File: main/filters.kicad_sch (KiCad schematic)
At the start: 104 parts, among them U36 TL071, U37 LM13700, U38 TL071, U39 TL071, U40 TL071, U41 LM13700, U42 LM13700, U43 LM13700

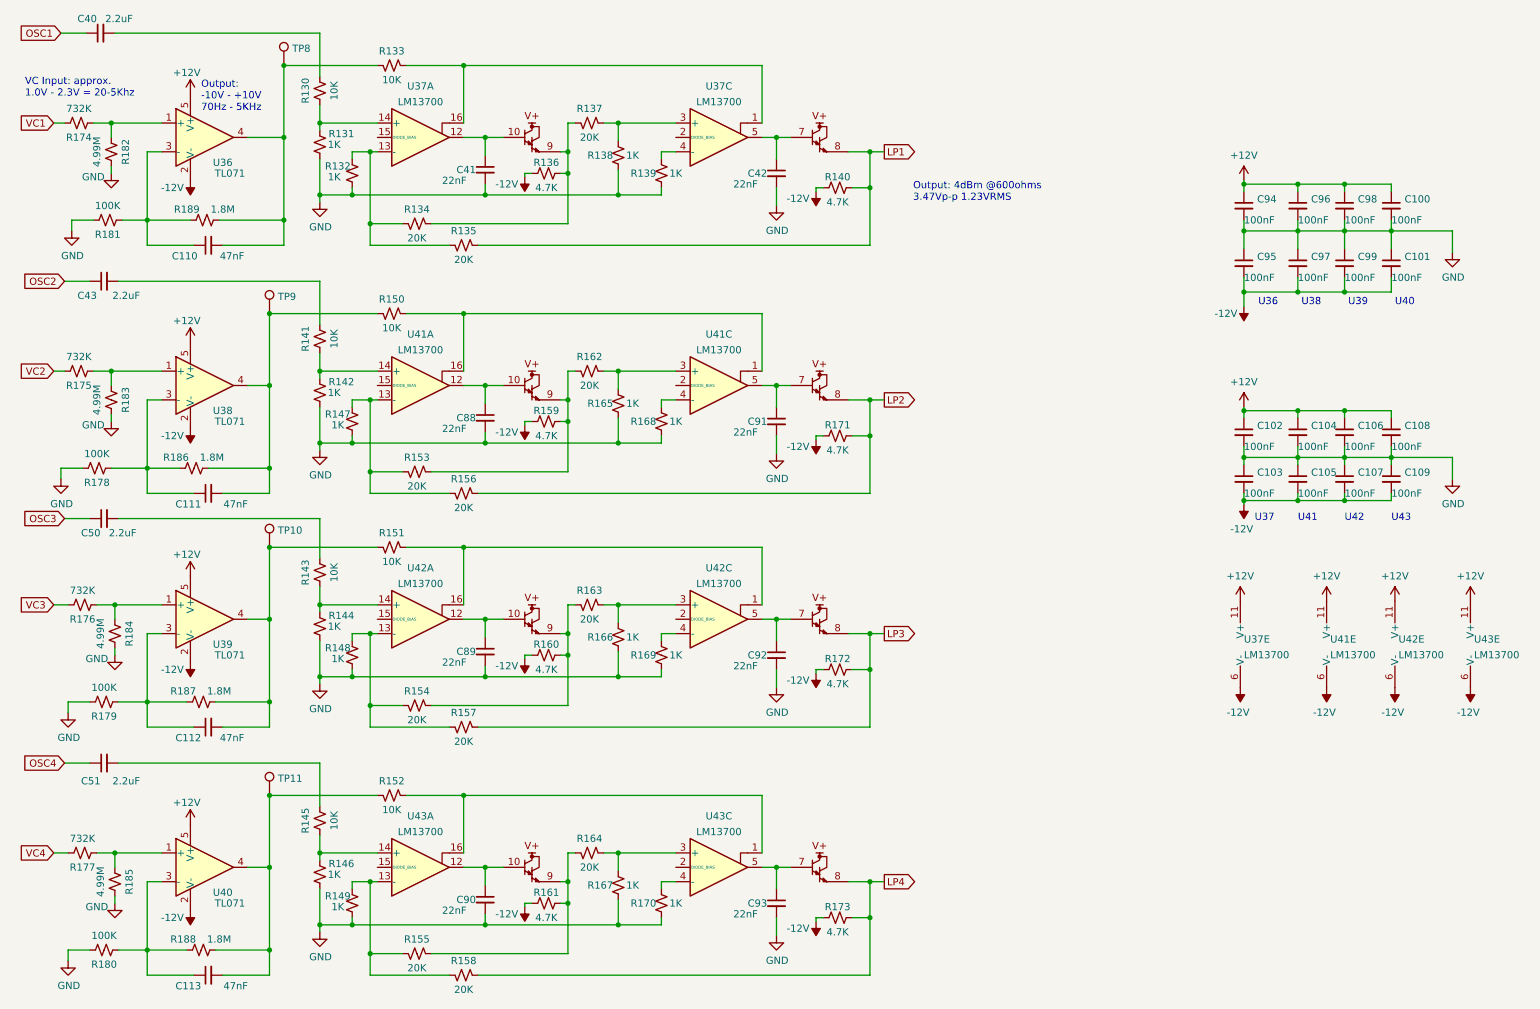
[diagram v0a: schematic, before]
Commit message: v1.0
Docs still need work.
Oscillators.sch not used. Saved just in case.
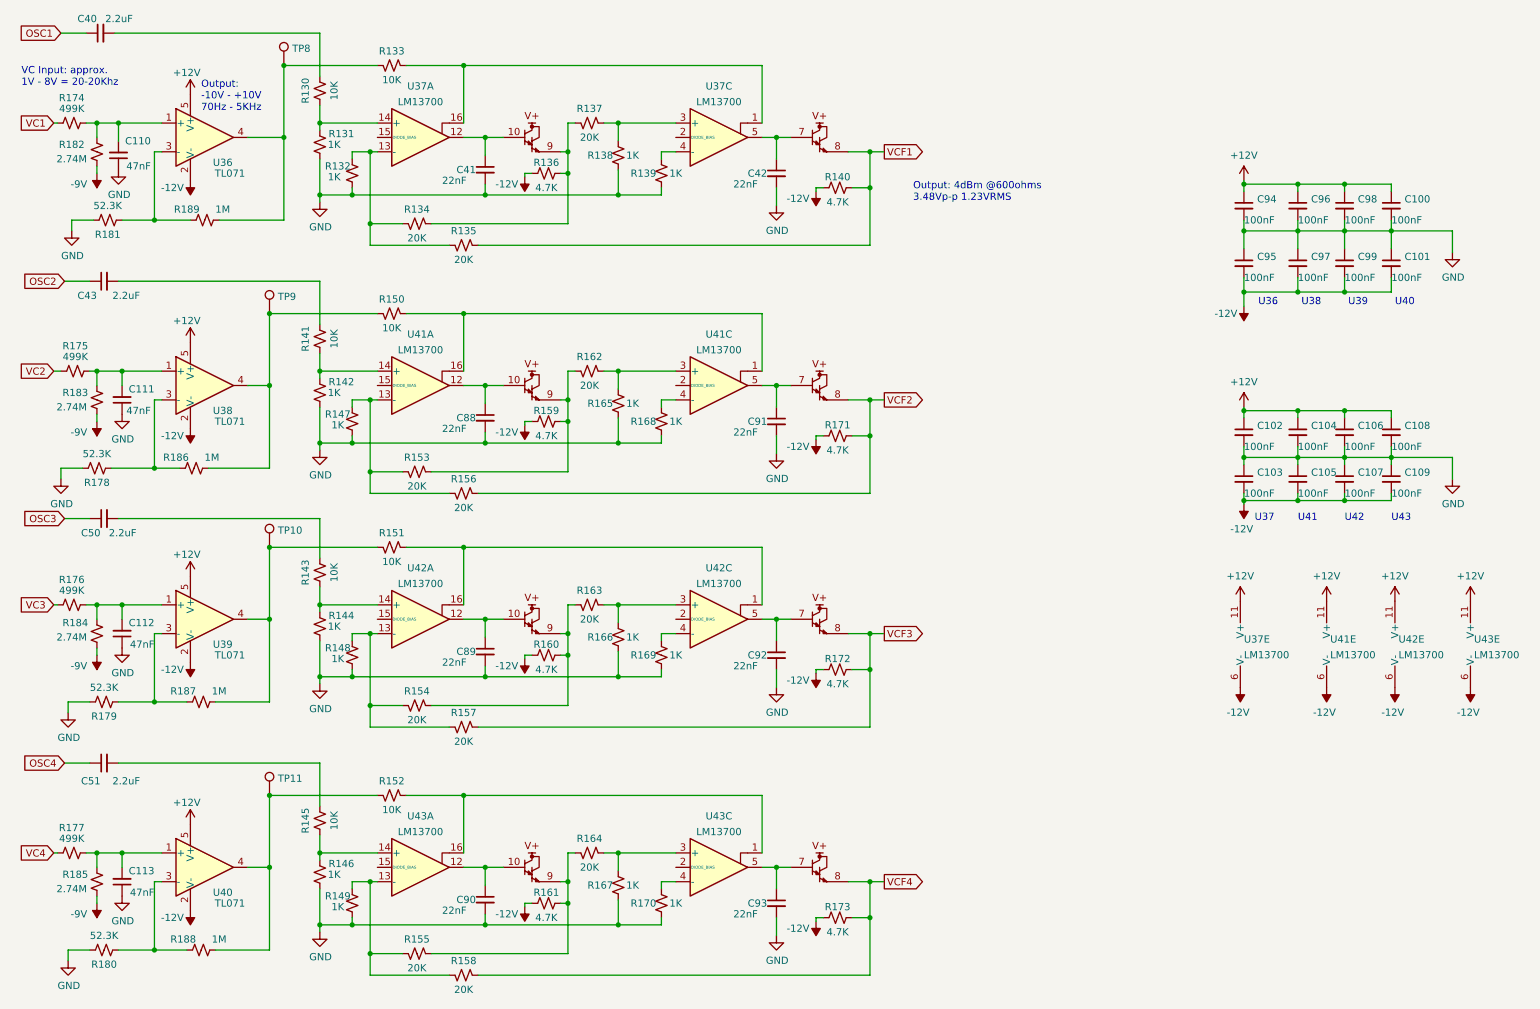
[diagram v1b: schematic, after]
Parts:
- C110, C111, C112, C113: footprint Capacitor_SMD:C_0805_2012Metric_Pad1.18x1.45mm_HandSolder -> Capacitor_SMD:C_0603_1608Metric_Pad1.08x0.95mm_HandSolder; LCSC Part # C53134 -> C1622
- R174, R175, R176, R177: value 732K -> 499K; LCSC Part # C218135 -> C131054
- R178, R179, R180, R181: value 100K -> 52.3K; LCSC Part # C25803 -> C23198
- R182, R183, R184, R185: value 4.99M -> 2.74M; LCSC Part # C2076722 -> C482806
- R186, R187, R188, R189: value 1.8M -> 1M; LCSC Part # C137772 -> C22935
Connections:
- net GND: now also C110.1, C111.1, C112.1, C113.1; no longer R182.1, R183.1, R184.1, R185.1
- net at R175.2, R183.2, U38.1 (+): now also C111.2
- net at R176.2, R184.2, U39.1 (+): now also C112.2
- net at R179.2, R187.1, U39.3 (-): no longer C112.1
- net at R151.1, R187.2, TP10.1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: no longer C112.2
- net at R150.1, R186.2, TP9.1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: no longer C111.2
- net at R178.2, R186.1, U38.3 (-): no longer C111.1
- net at R180.2, R188.1, U40.3 (-): no longer C113.1
- net at R152.1, R188.2, TP11.1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: no longer C113.2
- net at R133.1, R189.2, TP8.1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: no longer C110.2
- net at R177.2, R185.2, U40.1 (+): now also C113.2
- net at R174.2, R182.2, U36.1 (+): now also C110.2
- net at R181.2, R189.1, U36.3 (-): no longer C110.1
- net LP1 renamed VCF1
- net LP2 renamed VCF2
- net LP3 renamed VCF3
- net LP4 renamed VCF4
- new net -9V: R182.1, R183.1, R184.1, R185.1
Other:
- note added: "Output: 4dBm @600ohms 3.48Vp-p 1.23VRMS"
- note added: "VC Input: approx. 1V - 8V = 20-20Khz"
- note removed: "Output: 4dBm @600ohms 3.47Vp-p 1.23VRMS"
- note removed: "VC Input: approx. 1.0V - 2.3V = 20-5Khz"
- moved on the sheet: C110, C111, C112, C113, R174, R175, R176, R177, R182, R183, R184, R185

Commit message: Work in progress
Adds User Manual
Changes CV range to 0 - 8V
Adds spice vactrol test circuit.
Adds VCA spice study
Updates other spice and excel files.
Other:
- title: (none) -> Twangilizer
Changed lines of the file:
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@@
   (paper "A4")
   (title_block
-    (rev "1.0")
+    (title "Twangilizer")
+    (rev "1.1")
   )
   (junction (at 95.885 38.735) (diameter 0) (color 0 0 0 0)

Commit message: Latest gain plan.
Version 1.1
Sent to JLCPCB
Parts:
- added J13: Conn_01x02_Male, Connector_PinHeader_2.54mm:PinHeader_1x02_P2.54mm_Vertical, symbol Connector:Conn_01x02_Male
- C110, C111, C112, C113: value 47nF -> 22nF; LCSC Part # C1622 -> C21122
- C41, C42, C88, C89, C90, C91, C92, C93: LCSC Part # C415303 -> C77069
- R174, R175, R176, R177: value 499K -> 1M; LCSC Part # C131054 -> C22935
- R178, R179, R180, R181: value 52.3K -> 221K; LCSC Part # C23198 -> C326752
- R182, R183, R184, R185: value 2.74M -> 2.61M; LCSC Part # C482806 -> C482802
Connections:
- net at R150.1, TP9.1: now also J13.1 (Pin_1); no longer R186.2, U38.4
- new net: J13.2 (Pin_2), R186.2, U38.4

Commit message: Version 1.2
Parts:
- added C114, C115, C116, C117, C118, C119, C77, C9: 100nF, Capacitor_SMD:C_0603_1608Metric, symbol Device:C_Small
- added U2, U44, U45, U46: TL071, Package_TO_SOT_SMD:SOT-353_SC-70-5, symbol Amplifier_Operational:TLV172IDCK
- R178, R179, R180, R181: value 221K -> 205K; LCSC Part # C326752 -> C22949
- R182, R183, R184, R185: value 2.61M -> 2.55M; LCSC Part # C482802 -> C422950
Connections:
- net +12V: now also C114.1, C116.1, C118.1, C9.1, U2.5 (V+), U44.5 (V+), U45.5 (V+), U46.5 (V+)
- net -12V: now also C115.2, C117.2, C119.2, C77.2, U2.2 (V-), U44.2 (V-), U45.2 (V-), U46.2 (V-)
- net GND: now also C114.2, C115.1, C116.2, C117.1, C118.2, C119.1, C77.1, C9.2
- net VCF1: now also U2.3 (-), U2.4; no longer R135.2, R140.1, U37.8
- net VCF2: now also U44.3 (-), U44.4; no longer R156.2, R171.1, U41.8
- net VCF3: now also U45.3 (-), U45.4; no longer R157.2, R172.1, U42.8
- net VCF4: now also U46.3 (-), U46.4; no longer R158.2, R173.1, U43.8
- new net: R158.2, R173.1, U43.8, U46.1 (+)
- new net: R135.2, R140.1, U2.1 (+), U37.8
- new net: R157.2, R172.1, U42.8, U45.1 (+)
- new net: R156.2, R171.1, U41.8, U44.1 (+)
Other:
- note added: "Output: approx. -10V - +10V"
- note added: "U2"
- note added: "U44"
- note added: "U45"
- note added: "U46"
- note added: "VC Input: approx. 1V - 8V = 20-5Khz"
- note removed: "Output: -10V - +10V 70Hz - 5KHz"
- note removed: "VC Input: approx. 1V - 8V = 20-20Khz"
- moved on the sheet: C100, C101, C102, C103, C104, C105, C106, C107, C108, C109, C94, C95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
